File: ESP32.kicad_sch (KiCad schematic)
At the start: 12 parts, among them J2 Conn_01x02_Socket, U1 XC6206P332MR, U2 ESP32-C3FH4, U3 TYPE_C-CQ-111PWB, X1 CF4040M00015001

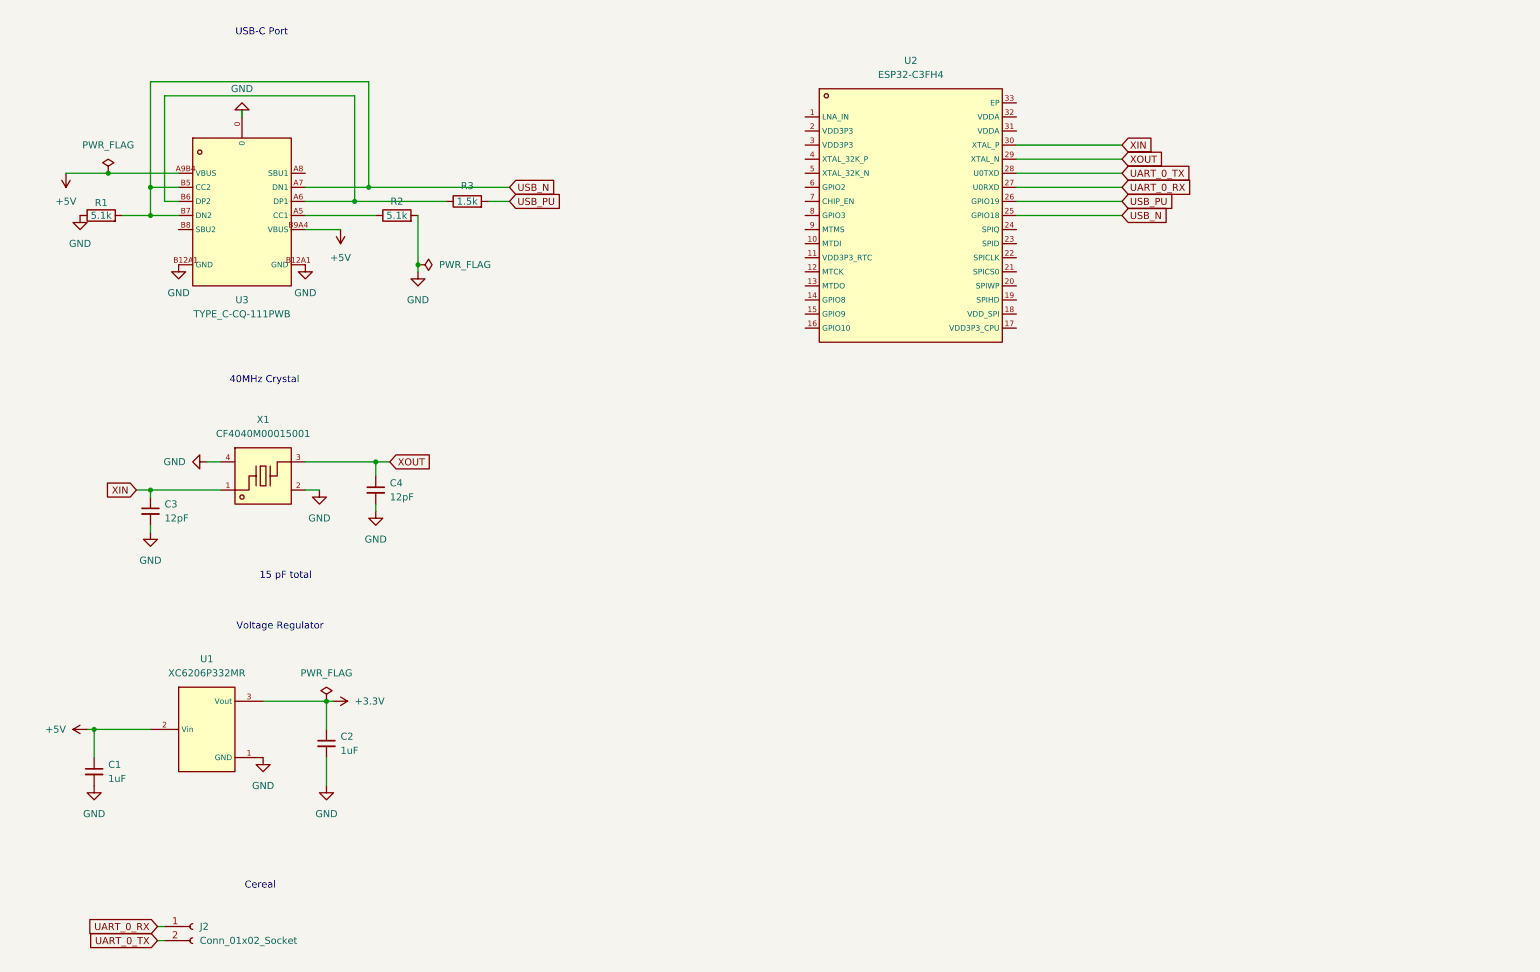
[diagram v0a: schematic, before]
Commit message: Finish wiring up ESP basics
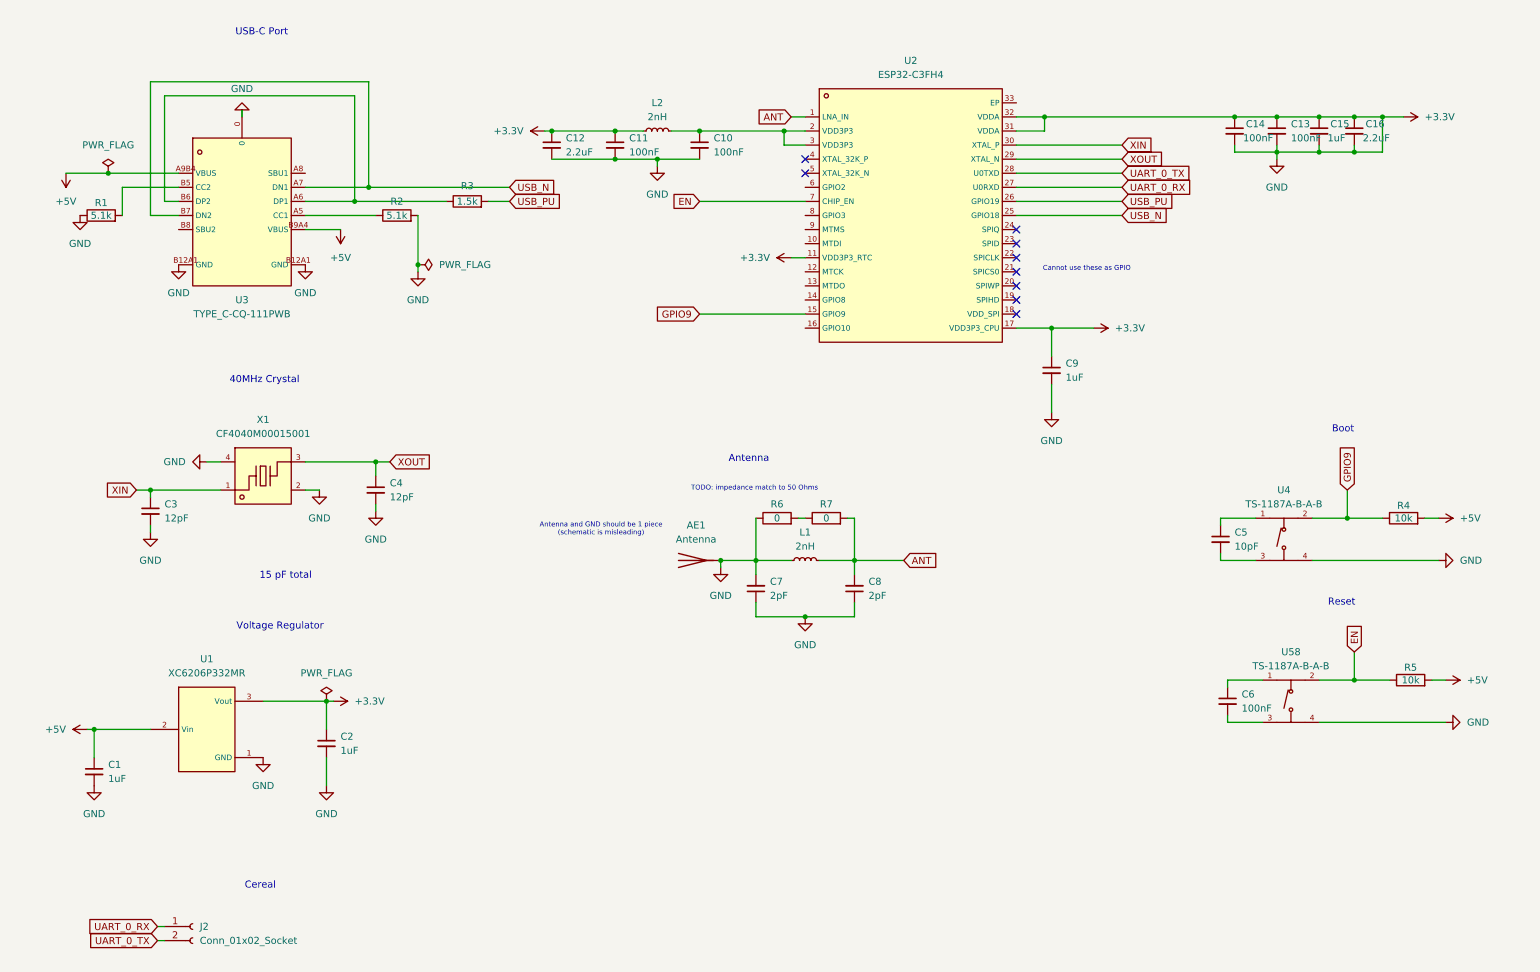
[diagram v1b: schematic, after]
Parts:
- added AE1: Antenna, symbol Device:Antenna
- added C10, C11, C13, C14, C6: 100nF, symbol Device:C_Small
- added C12, C16: 2.2uF, symbol Device:C_Small
- added C15, C9: 1uF, symbol Device:C_Small
- added C5: 10pF, symbol Device:C_Small
- added C7, C8: 2pF, symbol Device:C_Small
- added L1, L2: 2nH, symbol Device:L_Small
- added R4, R5: 10k, symbol Device:R
- added R6, R7: 0, symbol Device:R
- added U4, U58: TS-1187A-B-A-B, footprint:SW-SMD_4P-L5.1-W5.1-P3.70-LS6.5-TL-2, symbol TS-1187A-B-A-B:TS-1187A-B-A-B
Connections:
- net GND is gone; now on net +3.3V: C1.2, C2.2, C3.2, C4.2, R1.1, R2.2, U1.1 (GND), U3.0, U3.B12A1 (GND), X1.2 (GND), X1.4 (GND)
- net +3.3V: now also U2.11 (VDD3P3_RTC), U2.17 (VDD3P3_CPU), U2.31 (VDDA), U2.32 (VDDA), AE1.1 (A), C10.2, C11.1, C11.2, C12.1, C12.2, C13.1, C13.2, C14.1, C14.2, C15.1, C15.2, C16.1, C16.2, C7.1, C7.2, C8.1, C9.1, C9.2, L1.1, L2.1, R6.1, U4.4 (D), U58.4 (D)
- net +5V: now also R4.2, R5.2
- net USB_N: no longer R1.2, U3.B5 (CC2)
- net ANT: now reaches U2.1 (LNA_IN)
- net ANT: now also C8.2, L1.2, R7.2
- net GPIO9: now reaches U2.15 (GPIO9)
- net GPIO9: now also R4.1, U4.2 (B)
- net at U2.2 (VDD3P3): now also U2.3 (VDD3P3), C10.1, L2.2
- net EN: now reaches U2.7 (CHIP_EN)
- net EN: now also R5.1, U58.2 (B)
- new net: C6.1, U58.1 (A)
- new net: C6.2, U58.3 (C)
- new net: C5.1, U4.1 (A)
- new net: C5.2, U4.3 (C)
- new net: R6.2, R7.1
- new net: R1.2, U3.B5 (CC2)
- no-connect marks 0 -> 9
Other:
- note added: "Antenna"
- note added: "Antenna and GND should be 1 piece (schematic is misleading)"
- note added: "Boot"
- note added: "Cannot use these as GPIO"
- note added: "Reset"
- note added: "TODO: impedance match to 50 Ohms"

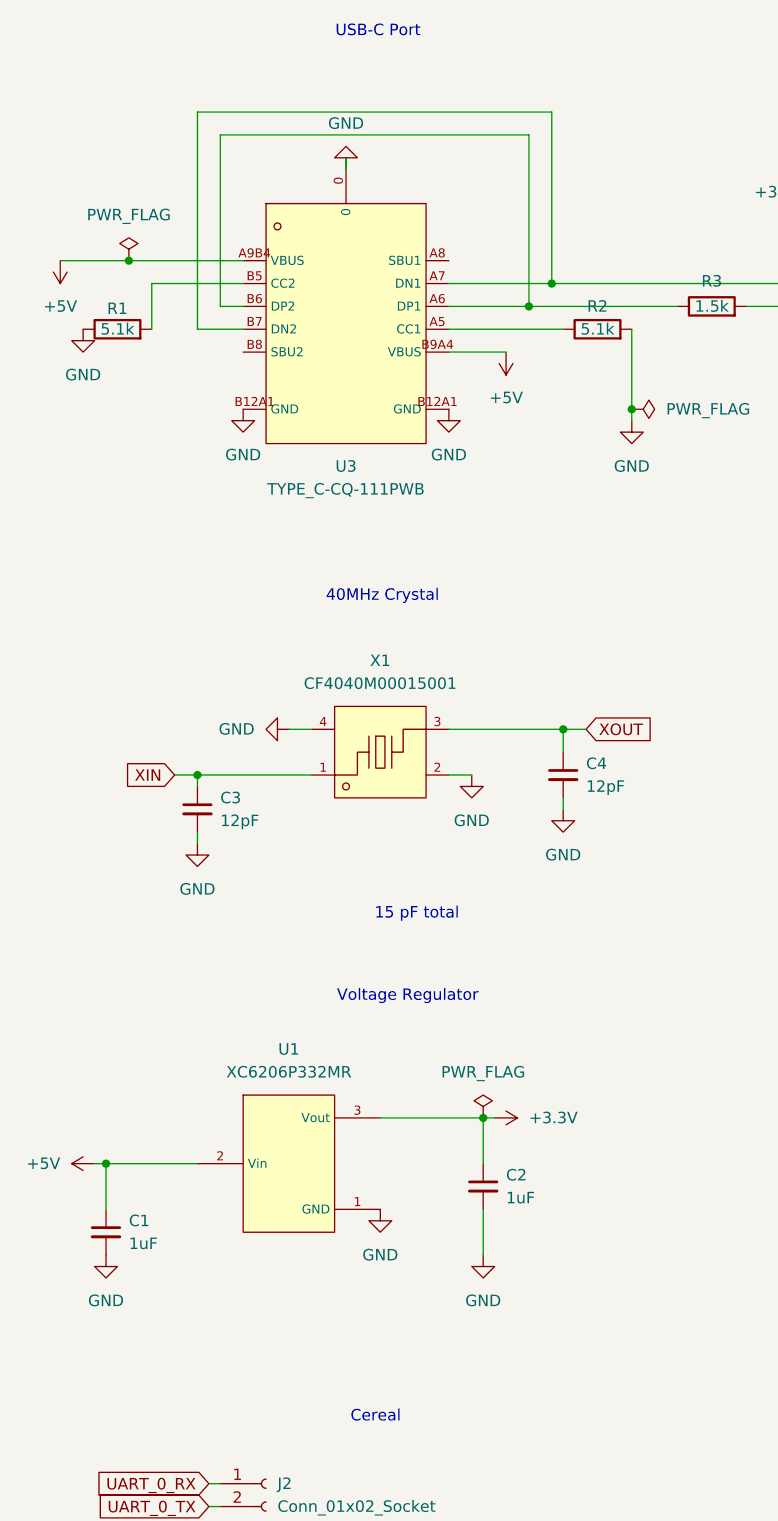
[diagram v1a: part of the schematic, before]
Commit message: Swap USB and LDO
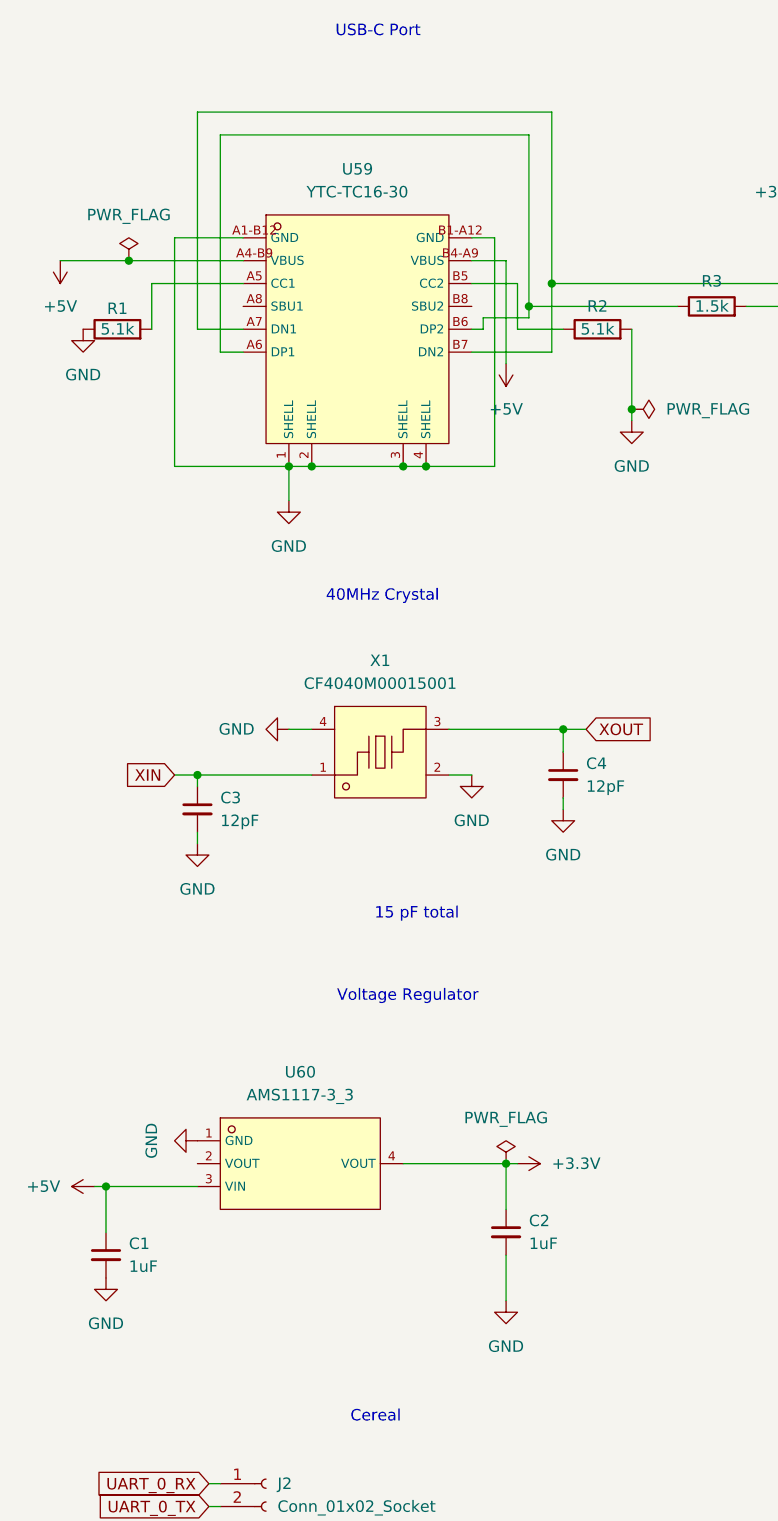
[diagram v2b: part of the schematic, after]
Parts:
- removed U1: XC6206P332MR, footprint:SOT-23-3_L2.9-W1.6-P1.90-LS2.8-BR, symbol XC6206P332MR:XC6206P332MR
- removed U3: TYPE_C-CQ-111PWB, footprint:USB-C-SMD_HC-TYPE-C-16P-CB1.6, symbol TYPE_C-CQ-111PWB:TYPE_C-CQ-111PWB
- added U59: YTC-TC16-30, footprint:USB-C-SMD_YIYUAN_YTC-TC16-30, symbol YTC-TC16-30:YTC-TC16-30
- added U60: AMS1117-3_3, footprint:SOT-223-3_L6.5-W3.4-P2.30-LS7.0-BR, symbol AMS1117-3_3:AMS1117-3_3
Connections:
- net +3.3V: now also U59.1 (SHELL), U59.2 (SHELL), U59.3 (SHELL), U59.4 (SHELL), U59.A1-B12 (GND), U59.B1-A12 (GND), U60.1 (GND), U60.4 (VOUT)
- net +5V: now also U59.A4-B9 (VBUS), U59.B4-A9 (VBUS), U60.3 (VIN)
- net USB_N: now also U59.A7 (DN1), U59.B7 (DN2)
- net at R2.1: now also U59.B5 (CC2)
- net at R3.1: now also U59.A6 (DP1), U59.B6 (DP2)
- net at R1.2: now also U59.A5 (CC1)
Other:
- moved on the sheet: C1, C2

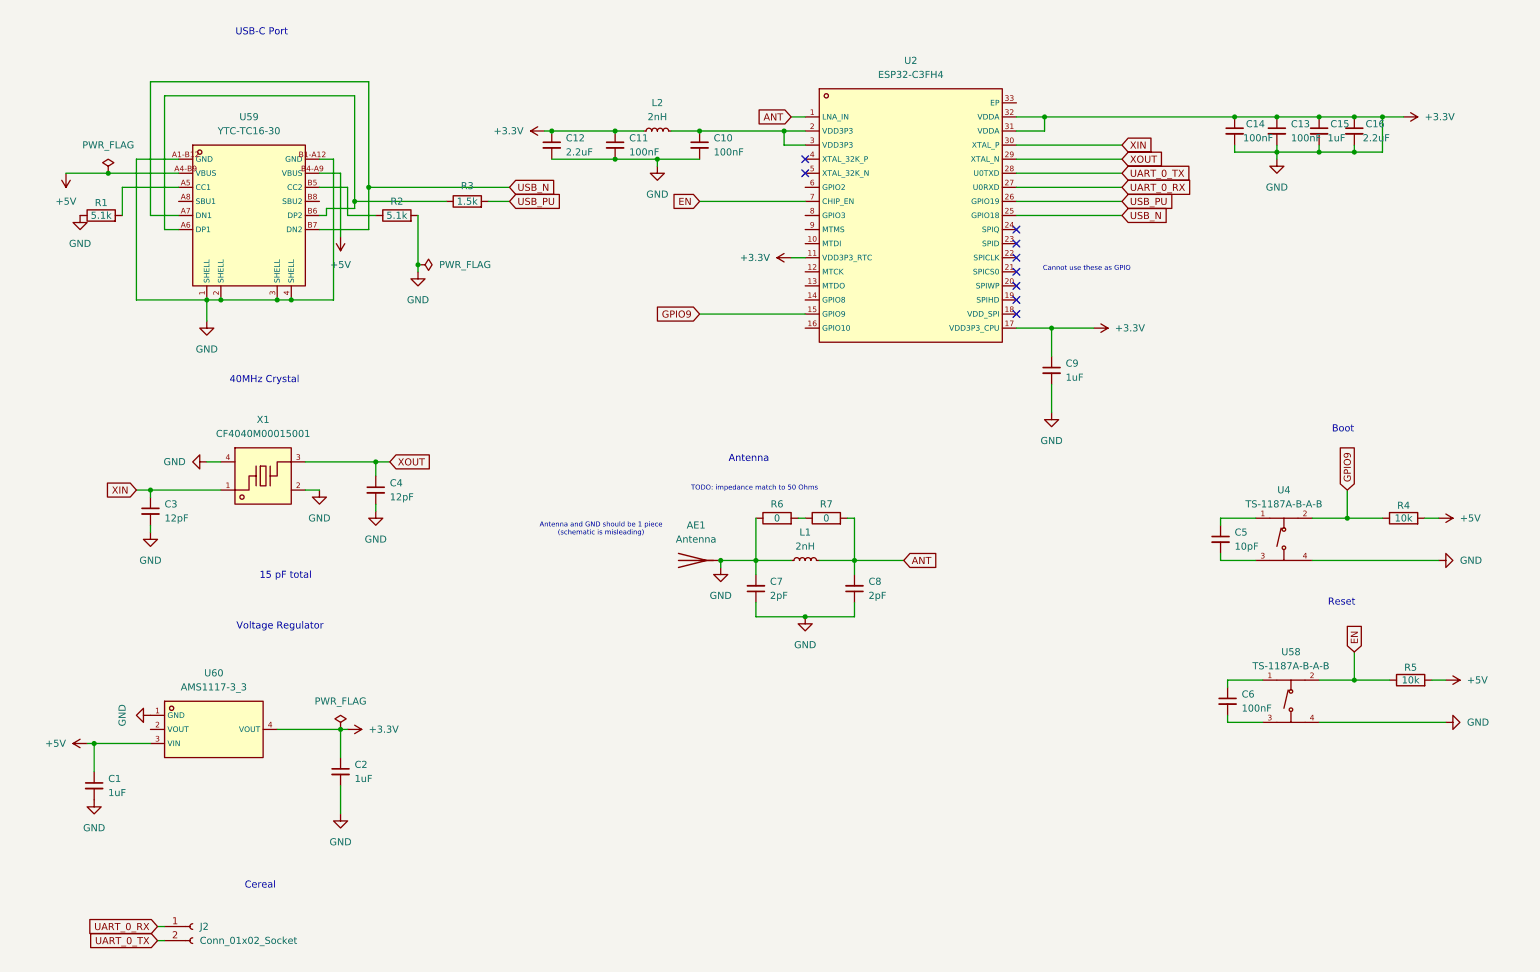
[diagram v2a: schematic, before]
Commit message: Break out remaining GPIO to labels, change UART to 1x4
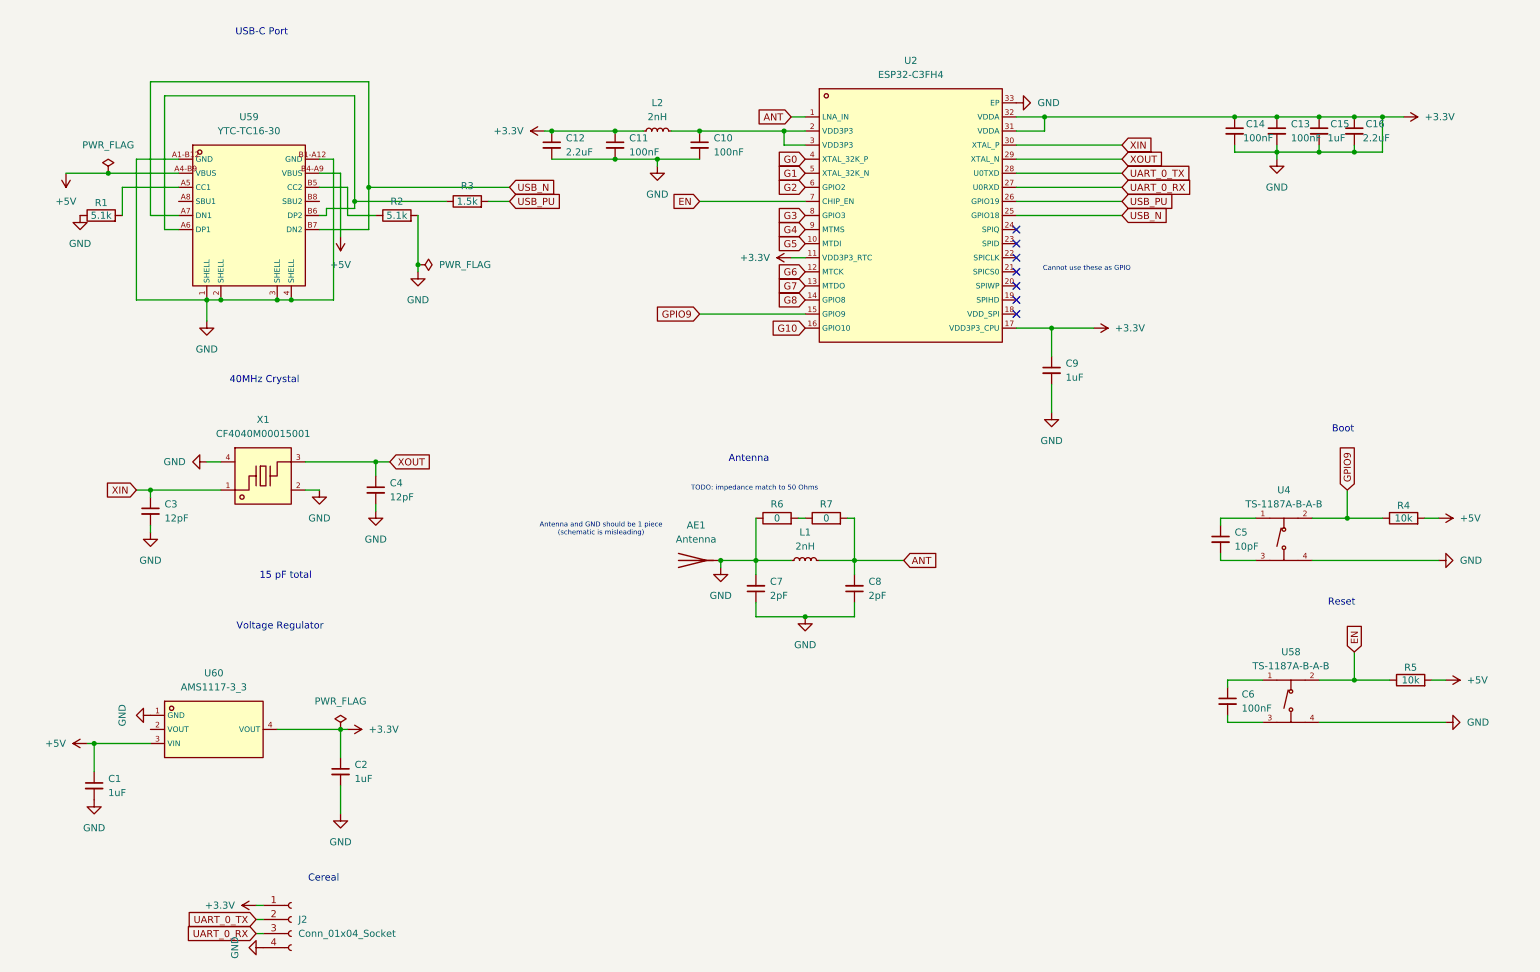
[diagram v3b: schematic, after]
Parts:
- removed J2: Conn_01x02_Socket, symbol Connector:Conn_01x02_Socket
- added J2: Conn_01x04_Socket, symbol Connector:Conn_01x04_Socket
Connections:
- net +3.3V: now also U2.33 (EP), J2.1 (Pin_1), J2.4 (Pin_4)
- net UART_0_RX: now also J2.3 (Pin_3)
- net UART_0_TX: now also J2.2 (Pin_2)
- net G5: now reaches U2.10 (MTDI)
- net G6: now reaches U2.12 (MTCK)
- net G7: now reaches U2.13 (MTDO)
- net G8: now reaches U2.14 (GPIO8)
- net G10: now reaches U2.16 (GPIO10)
- net G0: now reaches U2.4 (XTAL_32K_P)
- net G1: now reaches U2.5 (XTAL_32K_N)
- net G2: now reaches U2.6 (GPIO2)
- net G3: now reaches U2.8 (GPIO3)
- net G4: now reaches U2.9 (MTMS)
- no-connect marks 9 -> 7
